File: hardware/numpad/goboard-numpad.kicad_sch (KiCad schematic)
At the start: 5 parts

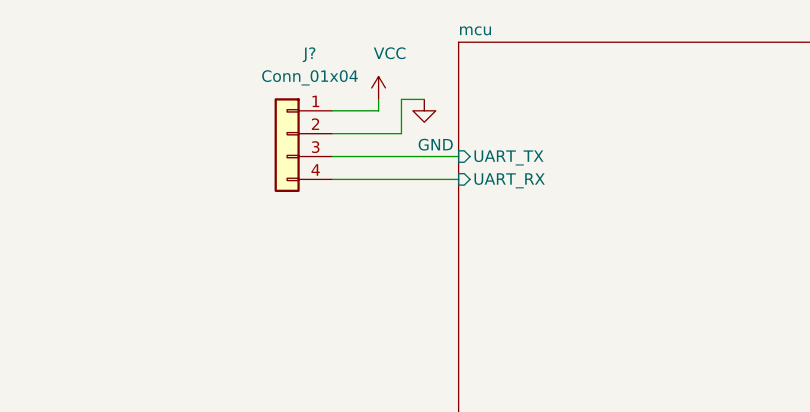
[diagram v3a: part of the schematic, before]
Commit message: Remove UART line from the NRF to the numpad
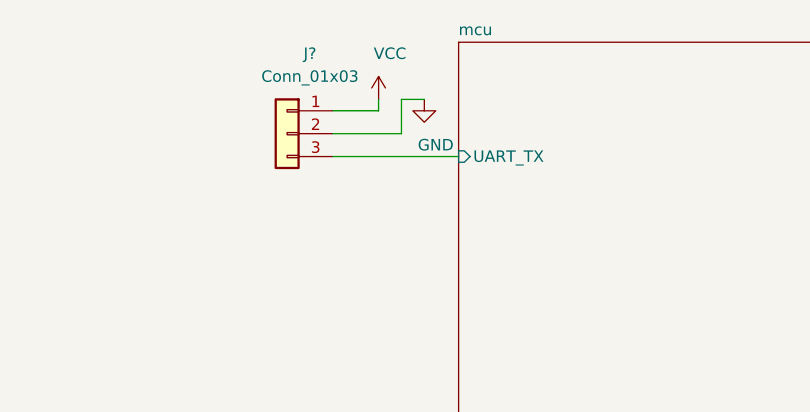
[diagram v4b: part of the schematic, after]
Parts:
- removed J?: Conn_01x04, symbol Connector_Generic:Conn_01x04
- added J?: Conn_01x03, symbol Connector_Generic:Conn_01x03
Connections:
- net GND: now also J?.2 (Pin_2)
- net VCC: now also J?.1 (Pin_1)
- net mcu/UART_TX: now also J?.3 (Pin_3)
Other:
- sheet mcu ports: added none; removed UART_RX
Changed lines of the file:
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@@
   (paper "A4")
   (junction (at 38.1 140.97) (diameter 0.9144) (color 0 0 0 0))
+  (no_connect (at 58.42 95.25))
+  (no_connect (at 45.72 95.25))
   (no_connect (at 45.72 100.33))
-  (no_connect (at 45.72 95.25))
-  (no_connect (at 58.42 95.25))
   (wire (pts (xy 31.75 140.97) (xy 38.1 140.97))
     (stroke (width 0) (type solid) (color 0 0 0 0))
@@
   )
   (wire (pts (xy 81.28 38.1) (xy 95.25 38.1))
-    (stroke (width 0) (type solid) (color 0 0 0 0))
-  )
-  (wire (pts (xy 81.28 40.64) (xy 95.25 40.64))
     (stroke (width 0) (type solid) (color 0 0 0 0))
   )
@@
     )
   )
-  (symbol (lib_id "Connector_Generic:Conn_01x04") (at 76.2 35.56 0) (mirror y) (unit 1)
+  (symbol (lib_id "Connector_Generic:Conn_01x03") (at 76.2 35.56 0) (mirror y) (unit 1)
     (in_bom yes) (on_board yes)
     (property "Reference" "J?" (id 0) (at 78.74 26.67 0))
-    (property "Value" "Conn_01x04" (id 1) (at 78.74 29.21 0))
+    (property "Value" "Conn_01x03" (id 1) (at 78.74 29.21 0))
     (property "Footprint" "" (id 2) (at 76.2 35.56 0)
       (effects (font (size 1.27 1.27)) hide)
@@
       (effects (font (size 1.27 1.27)) (justify right))
     )
-    (pin "UART_RX" input (at 95.25 40.64 180)
-      (effects (font (size 1.27 1.27)) (justify left))
-    )
   )
   (sheet_instances
@@
       (reference "J?") (unit 1) (value "Conn_02x05_Top_Bottom") (footprint "")
     )
-    (path "/3662dcb4-f1e1-45de-9873-3ddfde73b5db"
-      (reference "J?") (unit 1) (value "Conn_01x04") (footprint "")
+    (path "/6b328757-66f8-4e8e-8fe2-ee8e0f1f8e4b"
+      (reference "J?") (unit 1) (value "Conn_01x03") (footprint "")
     )
     (path "/f8d99eaa-eaec-4e45-8350-19b611a4fda8"

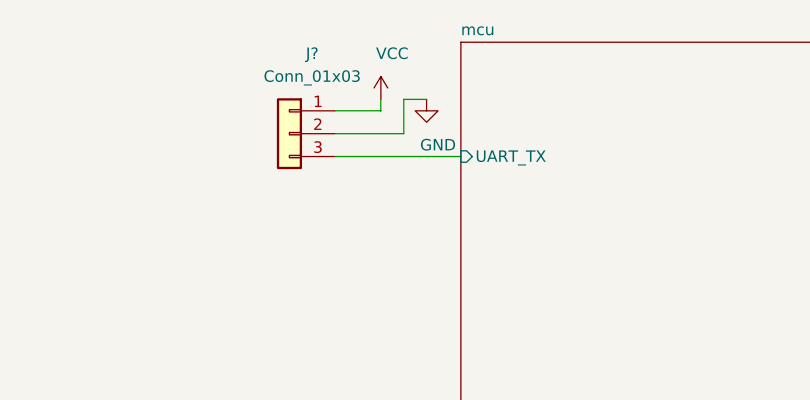
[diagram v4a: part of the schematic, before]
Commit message: Add a line for the UART direction main->numpad
This is necessary as the numlock-led is situated on the numpad and the
main mcu has to be able to switch it on and off.
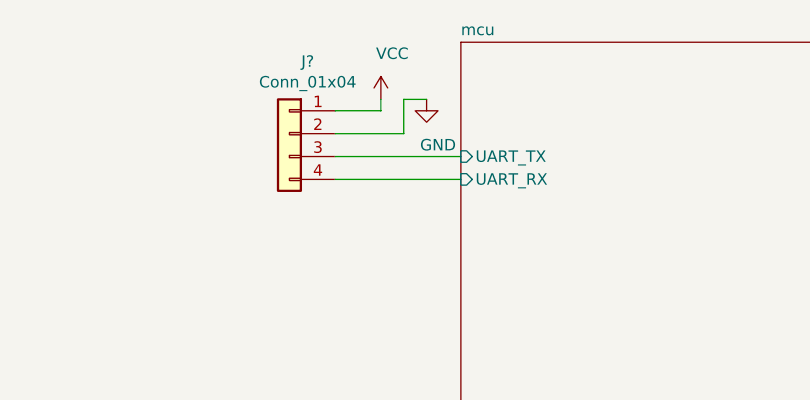
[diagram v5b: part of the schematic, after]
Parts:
- removed J?: Conn_01x03, symbol Connector_Generic:Conn_01x03
- added J?: Conn_01x04, symbol Connector_Generic:Conn_01x04
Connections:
- net GND: now also J?.2 (Pin_2)
- net VCC: now also J?.1 (Pin_1)
- net mcu/UART_TX: now also J?.3 (Pin_3)
- new net mcu/UART_RX: J?.4 (Pin_4)
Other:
- sheet mcu ports: added UART_RX; removed none
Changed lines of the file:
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@@
   (paper "A4")
   (junction (at 38.1 140.97) (diameter 0.9144) (color 0 0 0 0))
+  (no_connect (at 45.72 95.25))
   (no_connect (at 58.42 95.25))
-  (no_connect (at 45.72 95.25))
   (no_connect (at 45.72 100.33))
   (wire (pts (xy 31.75 140.97) (xy 38.1 140.97))
@@
   )
   (wire (pts (xy 81.28 38.1) (xy 95.25 38.1))
+    (stroke (width 0) (type solid) (color 0 0 0 0))
+  )
+  (wire (pts (xy 81.28 40.64) (xy 95.25 40.64))
     (stroke (width 0) (type solid) (color 0 0 0 0))
   )
@@
     )
   )
-  (symbol (lib_id "Connector_Generic:Conn_01x03") (at 76.2 35.56 0) (mirror y) (unit 1)
-    (in_bom yes) (on_board yes)
-    (property "Reference" "J?" (id 0) (at 78.74 26.67 0))
-    (property "Value" "Conn_01x03" (id 1) (at 78.74 29.21 0))
+  (symbol (lib_id "Connector_Generic:Conn_01x04") (at 76.2 35.56 0) (mirror y) (unit 1)
+    (in_bom yes) (on_board yes)
+    (property "Reference" "J?" (id 0) (at 78.232 27.5398 0))
+    (property "Value" "Conn_01x04" (id 1) (at 78.232 29.8385 0))
     (property "Footprint" "" (id 2) (at 76.2 35.56 0)
       (effects (font (size 1.27 1.27)) hide)
@@
       (effects (font (size 1.27 1.27)) (justify right))
     )
+    (pin "UART_RX" input (at 95.25 40.64 180)
+      (effects (font (size 1.27 1.27)) (justify left))
+    )
   )
   (sheet_instances
@@
       (reference "J?") (unit 1) (value "Conn_02x05_Top_Bottom") (footprint "")
     )
-    (path "/6b328757-66f8-4e8e-8fe2-ee8e0f1f8e4b"
-      (reference "J?") (unit 1) (value "Conn_01x03") (footprint "")
+    (path "/3e6f4865-3bc2-43e6-a156-c9674a4aeea4"
+      (reference "J?") (unit 1) (value "Conn_01x04") (footprint "")
     )
     (path "/f8d99eaa-eaec-4e45-8350-19b611a4fda8"

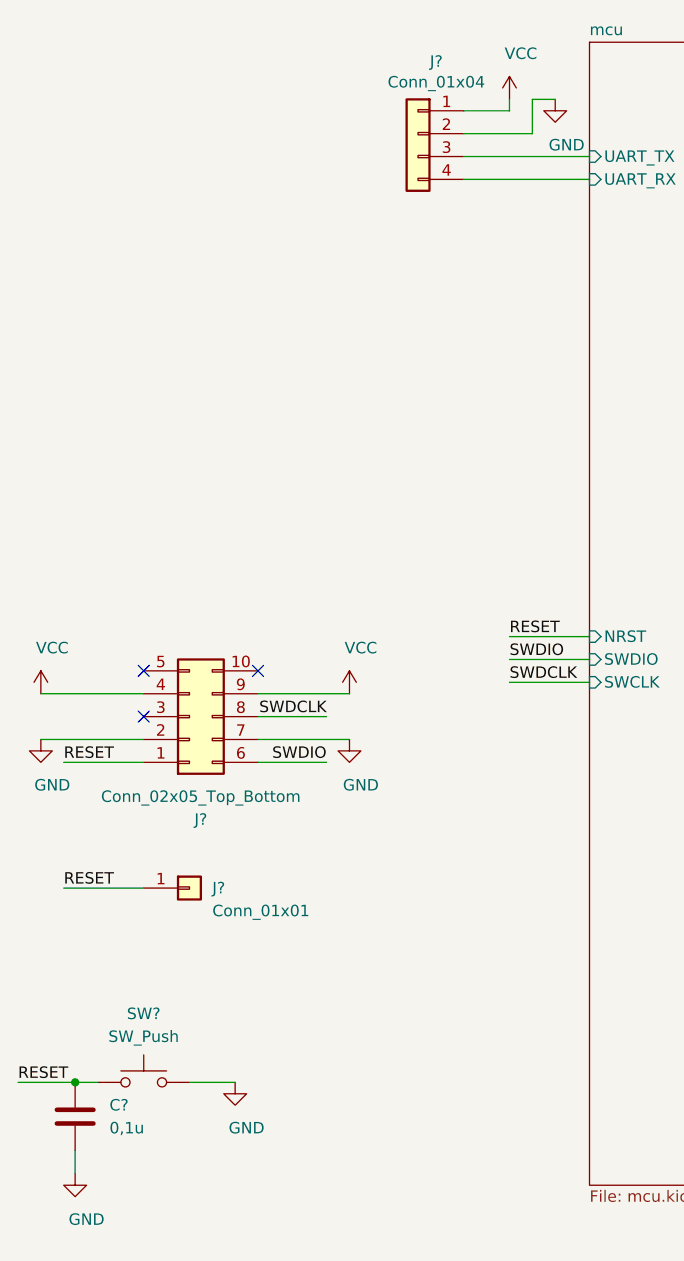
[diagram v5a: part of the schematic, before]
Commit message: Add first rough version of the numpad PCB
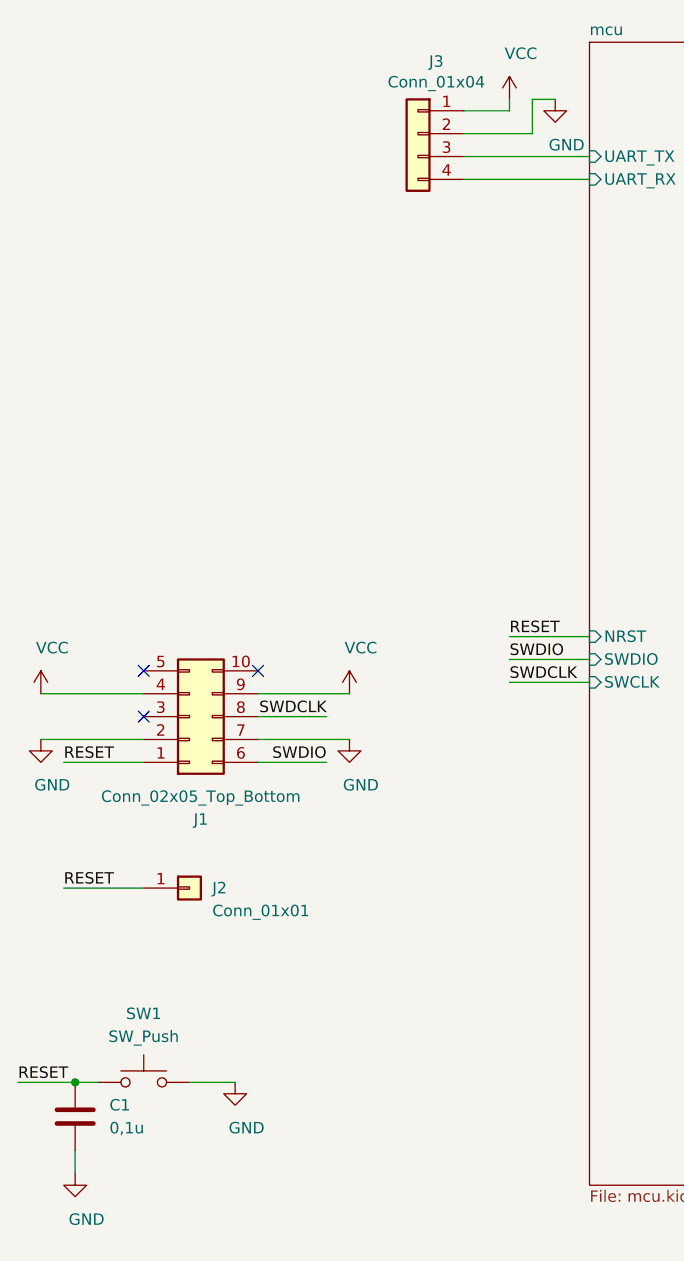
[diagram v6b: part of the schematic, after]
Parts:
- C1: renamed from C?; footprint (none) -> Capacitor_SMD:C_0603_1608Metric_Pad1.08x0.95mm_HandSolder
- J1: renamed from J?; footprint (none) -> footprints:programming_port_st_link_clone
- J2: renamed from J?; footprint (none) -> Connector_PinHeader_2.54mm:PinHeader_1x01_P2.54mm_Vertical
- gave numbers to parts that had none: 2

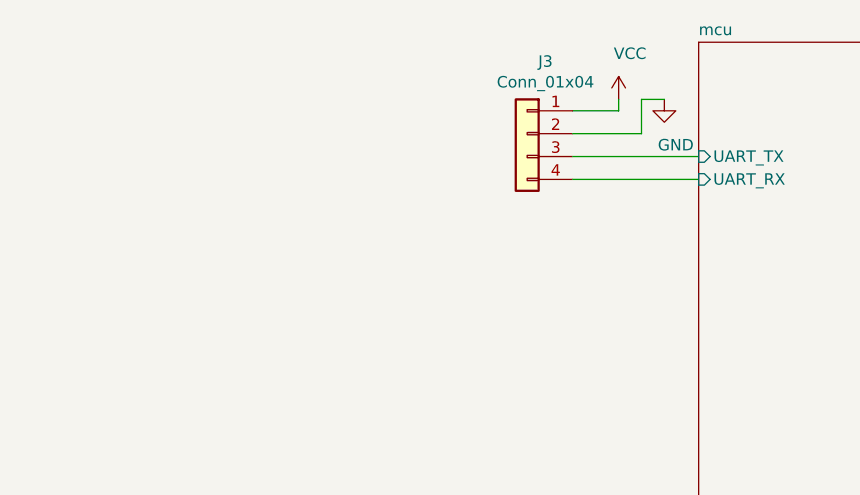
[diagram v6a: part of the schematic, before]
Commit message: Update the connection of the numpad
The ID line is added to the numpad side and the connector pin assignment
is updated.
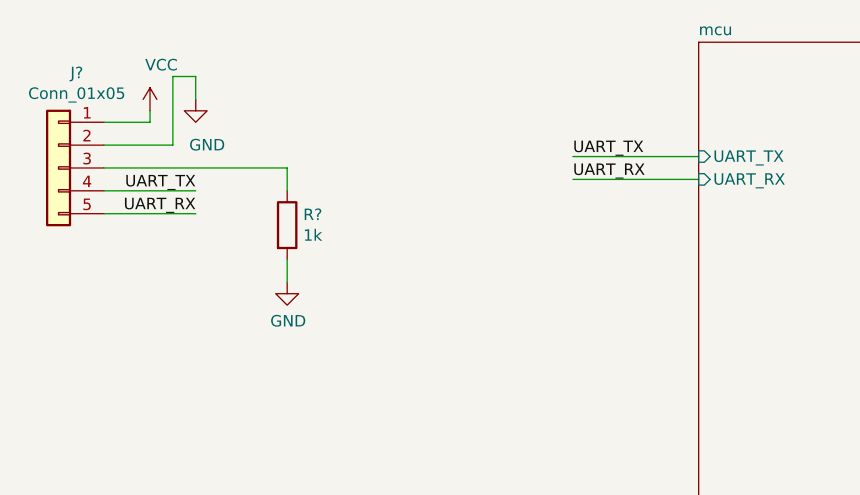
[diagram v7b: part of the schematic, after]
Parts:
- removed J3: Conn_01x04, symbol Connector_Generic:Conn_01x04
- added J?: Conn_01x05, symbol Connector_Generic:Conn_01x05
- added R?: 1k, Resistor_SMD:R_0603_1608Metric_Pad0.98x0.95mm_HandSolder, symbol Device:R
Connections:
- net GND: now also J?.2 (Pin_2), R?.2
- net VCC: now also J?.1 (Pin_1)
- new net: J?.3 (Pin_3), R?.1
- new net UART_RX: J?.5 (Pin_5)
- new net UART_TX: J?.4 (Pin_4)

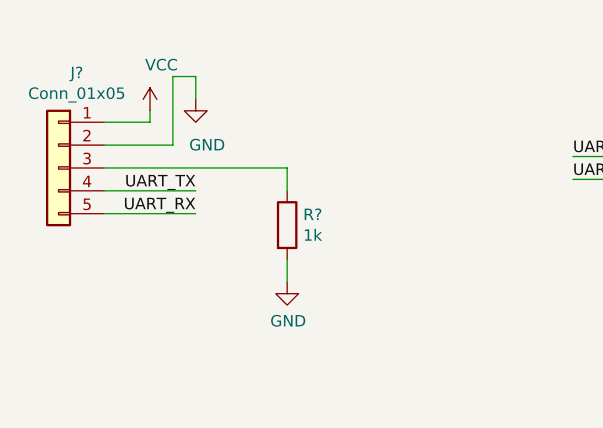
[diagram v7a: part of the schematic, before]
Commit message: Add footprints to two components
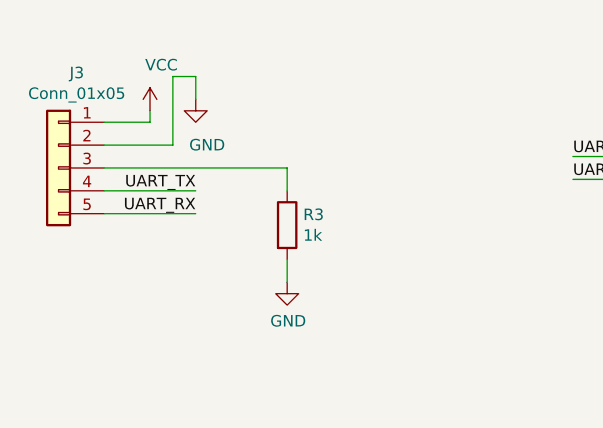
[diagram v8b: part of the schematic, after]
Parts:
- J3: renamed from J?; footprint (none) -> Connector_PinHeader_2.54mm:PinHeader_1x05_P2.54mm_Vertical
- SW1: footprint (none) -> Button_Switch_SMD:SW_SPST_CK_RS282G05A3
- gave numbers to parts that had none: 1
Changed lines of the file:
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@@
-(kicad_sch (version 20210123) (generator eeschema)
+(kicad_sch (version 20210126) (generator eeschema)
   (paper "A4")
   (junction (at 38.1 140.97) (diameter 0.9144) (color 0 0 0 0))
@@
       (effects (font (size 1.27 1.27)) hide)
     )
+    (pin "1")
   )
   (symbol (lib_id "power:VCC") (at 34.29 97.79 0) (unit 1)
@@
       (effects (font (size 1.27 1.27)) hide)
     )
+    (pin "1")
   )
   (symbol (lib_id "power:VCC") (at 68.58 97.79 0) (unit 1)
@@
       (effects (font (size 1.27 1.27)) hide)
     )
+    (pin "1")
   )
   (symbol (lib_id "power:GND") (at 34.29 102.87 0) (unit 1)
@@
       (effects (font (size 1.27 1.27)) hide)
     )
+    (pin "1")
   )
   (symbol (lib_id "power:GND") (at 38.1 151.13 0) (unit 1)
@@
       (effects (font (size 1.27 1.27)) hide)
     )
+    (pin "1")
   )
   (symbol (lib_id "power:GND") (at 39.37 31.75 0) (unit 1)
@@
       (effects (font (size 1.27 1.27)) hide)
     )
+    (pin "1")
   )
   (symbol (lib_id "power:GND") (at 49.53 52.07 0) (unit 1)
     (in_bom yes) (on_board yes)
-    (property "Reference" "#PWR?" (id 0) (at 49.53 58.42 0)
+    (property "Reference" "#PWR0113" (id 0) (at 49.53 58.42 0)
       (effects (font (size 1.27 1.27)) hide)
     )
@@
       (effects (font (size 1.27 1.27)) hide)
     )
+    (pin "1")
   )
   (symbol (lib_id "power:GND") (at 55.88 140.97 0) (unit 1)
@@
       (effects (font (size 1.27 1.27)) hide)
     )
+    (pin "1")
   )
   (symbol (lib_id "power:GND") (at 68.58 102.87 0) (unit 1)
@@
       (effects (font (size 1.27 1.27)) hide)
     )
+    (pin "1")
   )
   (symbol (lib_id "Device:R") (at 49.53 45.72 0) (unit 1)
     (in_bom yes) (on_board yes)
-    (property "Reference" "R?" (id 0) (at 51.3081 44.5706 0)
+    (property "Reference" "R3" (id 0) (at 51.3081 44.5706 0)
       (effects (font (size 1.27 1.27)) (justify left))
     )
@@
       (effects (font (size 1.27 1.27)) hide)
     )
+    (pin "1")
+    (pin "2")
   )
   (symbol (lib_id "Connector_Generic:Conn_01x01") (at 50.8 119.38 0) (unit 1)
@@
       (effects (font (size 1.27 1.27)) hide)
     )
+    (pin "1")
   )
   (symbol (lib_id "Device:C") (at 38.1 144.78 0) (unit 1)
@@
       (effects (font (size 1.27 1.27)) hide)
     )
+    (pin "1")
+    (pin "2")
   )
   (symbol (lib_id "Switch:SW_Push") (at 45.72 140.97 0) (unit 1)
@@
     (property "Reference" "SW1" (id 0) (at 45.72 133.35 0))
     (property "Value" "SW_Push" (id 1) (at 45.72 135.89 0))
-    (property "Footprint" "" (id 2) (at 45.72 135.89 0)
+    (property "Footprint" "Button_Switch_SMD:SW_SPST_CK_RS282G05A3" (id 2) (at 45.72 135.89 0)
       (effects (font (size 1.27 1.27)) hide)
     )
@@
       (effects (font (size 1.27 1.27)) hide)
     )
+    (pin "1")
+    (pin "2")
   )
   (symbol (lib_id "Connector_Generic:Conn_01x05") (at 24.13 39.37 0) (mirror y) (unit 1)
     (in_bom yes) (on_board yes)
-    (property "Reference" "J?" (id 0) (at 26.162 28.8098 0))
+    (property "Reference" "J3" (id 0) (at 26.162 28.8098 0))
     (property "Value" "Conn_01x05" (id 1) (at 26.162 31.1085 0))
-    (property "Footprint" "" (id 2) (at 24.13 39.37 0)
+    (property "Footprint" "Connector_PinHeader_2.54mm:PinHeader_1x05_P2.54mm_Vertical" (id 2) (at 24.13 39.37 0)
       (effects (font (size 1.27 1.27)) hide)
     )
@@
       (effects (font (size 1.27 1.27)) hide)
     )
+    (pin "1")
+    (pin "2")
+    (pin "3")
+    (pin "4")
+    (pin "5")
   )
   (symbol (lib_id "Connector_Generic:Conn_02x05_Top_Bottom") (at 50.8 100.33 0) (mirror x) (unit 1)
@@
       (effects (font (size 1.27 1.27)) hide)
     )
+    (pin "1")
+    (pin "10")
+    (pin "2")
+    (pin "3")
+    (pin "4")
+    (pin "5")
+    (pin "6")
+    (pin "7")
+    (pin "8")
+    (pin "9")
   )
   (sheet (at 180.34 25.4) (size 53.34 130.81)
@@
     )
     (path "/e7b45c0c-ec1c-4549-9c6c-81ed0b0da2f5"
-      (reference "#PWR?") (unit 1) (value "GND") (footprint "")
+      (reference "#PWR0113") (unit 1) (value "GND") (footprint "")
     )
     (path "/07e3d3ae-4259-4c4b-b7e9-b71a69d216b3"
@@
     )
     (path "/2aaa1463-c439-4735-8359-1fc80c6092e7"
-      (reference "J?") (unit 1) (value "Conn_01x05") (footprint "")
+      (reference "J3") (unit 1) (value "Conn_01x05") (footprint "Connector_PinHeader_2.54mm:PinHeader_1x05_P2.54mm_Vertical")
     )
     (path "/480f8756-d1de-4a1e-92bf-b0bdd56c4c78"
-      (reference "R?") (unit 1) (value "1k") (footprint "Resistor_SMD:R_0603_1608Metric_Pad0.98x0.95mm_HandSolder")
+      (reference "R3") (unit 1) (value "1k") (footprint "Resistor_SMD:R_0603_1608Metric_Pad0.98x0.95mm_HandSolder")
     )
     (path "/9efc1083-5914-419f-bcd0-741b18f0726c"
-      (reference "SW1") (unit 1) (value "SW_Push") (footprint "")
+      (reference "SW1") (unit 1) (value "SW_Push") (footprint "Button_Switch_SMD:SW_SPST_CK_RS282G05A3")
+    )
+    (path "/7cad715e-ebc0-41a5-9955-927ca63abd2f/496c40c2-41af-4714-9774-9ec038cfce72"
+      (reference "#PWR0114") (unit 1) (value "VCC") (footprint "")
     )
     (path "/7cad715e-ebc0-41a5-9955-927ca63abd2f/1f1640c3-d0af-48b7-bf24-2dc886f8490e"
@@
       (reference "D10") (unit 1) (value "BAT54C") (footprint "Package_TO_SOT_SMD:SOT-23")
     )
+    (path "/7cad715e-ebc0-41a5-9955-927ca63abd2f/2793fa1a-5f28-4765-a26a-d4a92a80fdd4"
+      (reference "R4") (unit 1) (value "100k") (footprint "Resistor_SMD:R_0603_1608Metric_Pad0.98x0.95mm_HandSolder")
+    )
+    (path "/7cad715e-ebc0-41a5-9955-927ca63abd2f/3a75d442-442c-4b22-9144-12a227e61aec"
+      (reference "R5") (unit 1) (value "100k") (footprint "Resistor_SMD:R_0603_1608Metric_Pad0.98x0.95mm_HandSolder")
+    )
+    (path "/7cad715e-ebc0-41a5-9955-927ca63abd2f/50bcdd0d-18db-4cd9-8fda-21c8a8a87e1d"
+      (reference "R6") (unit 1) (value "100k") (footprint "Resistor_SMD:R_0603_1608Metric_Pad0.98x0.95mm_HandSolder")
+    )
+    (path "/7cad715e-ebc0-41a5-9955-927ca63abd2f/4bd849d9-ce34-4618-997c-86f4f4ef8873"
+      (reference "R7") (unit 1) (value "100k") (footprint "Resistor_SMD:R_0603_1608Metric_Pad0.98x0.95mm_HandSolder")
+    )
     (path "/7cad715e-ebc0-41a5-9955-927ca63abd2f/e26be467-73d8-4d75-9608-e56cc8613f7a"
